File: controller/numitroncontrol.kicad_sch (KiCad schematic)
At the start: 10 parts, among them J0 Screw_Terminal_01x02, J1 Conn_01x06, J2 Conn_01x06, J3 RTC, J4 GPS, U1 LM317_TO-220

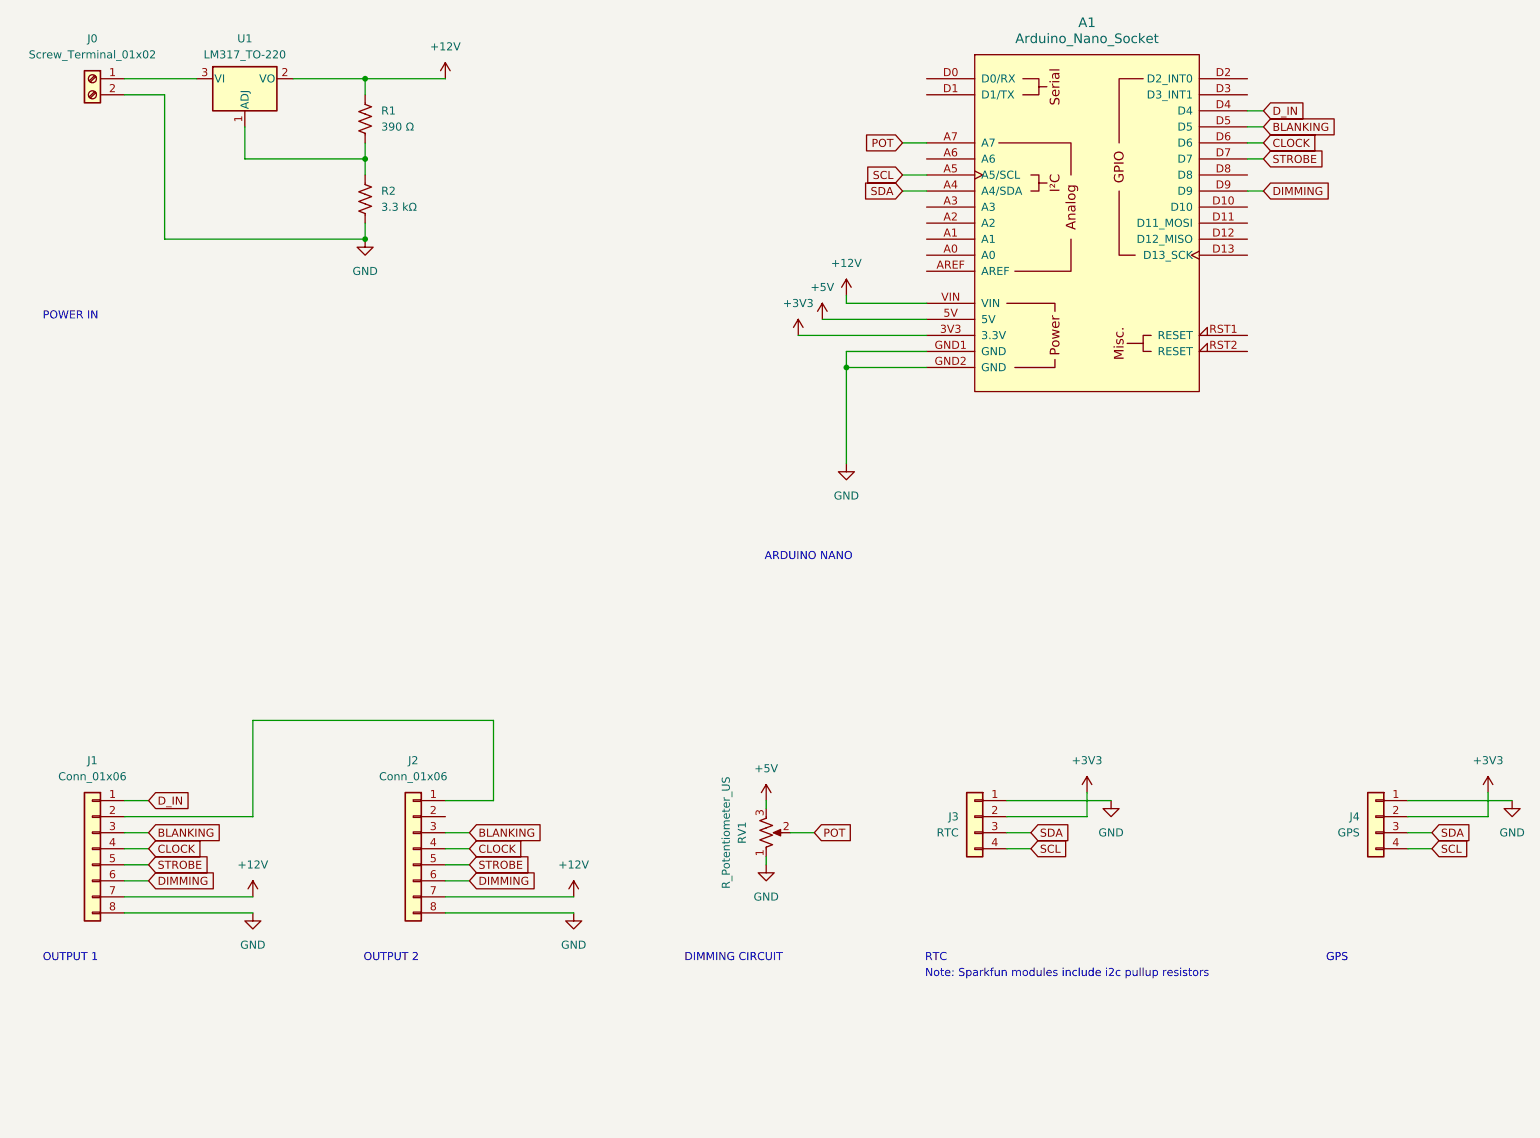
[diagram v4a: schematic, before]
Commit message: fixed serial communication pins
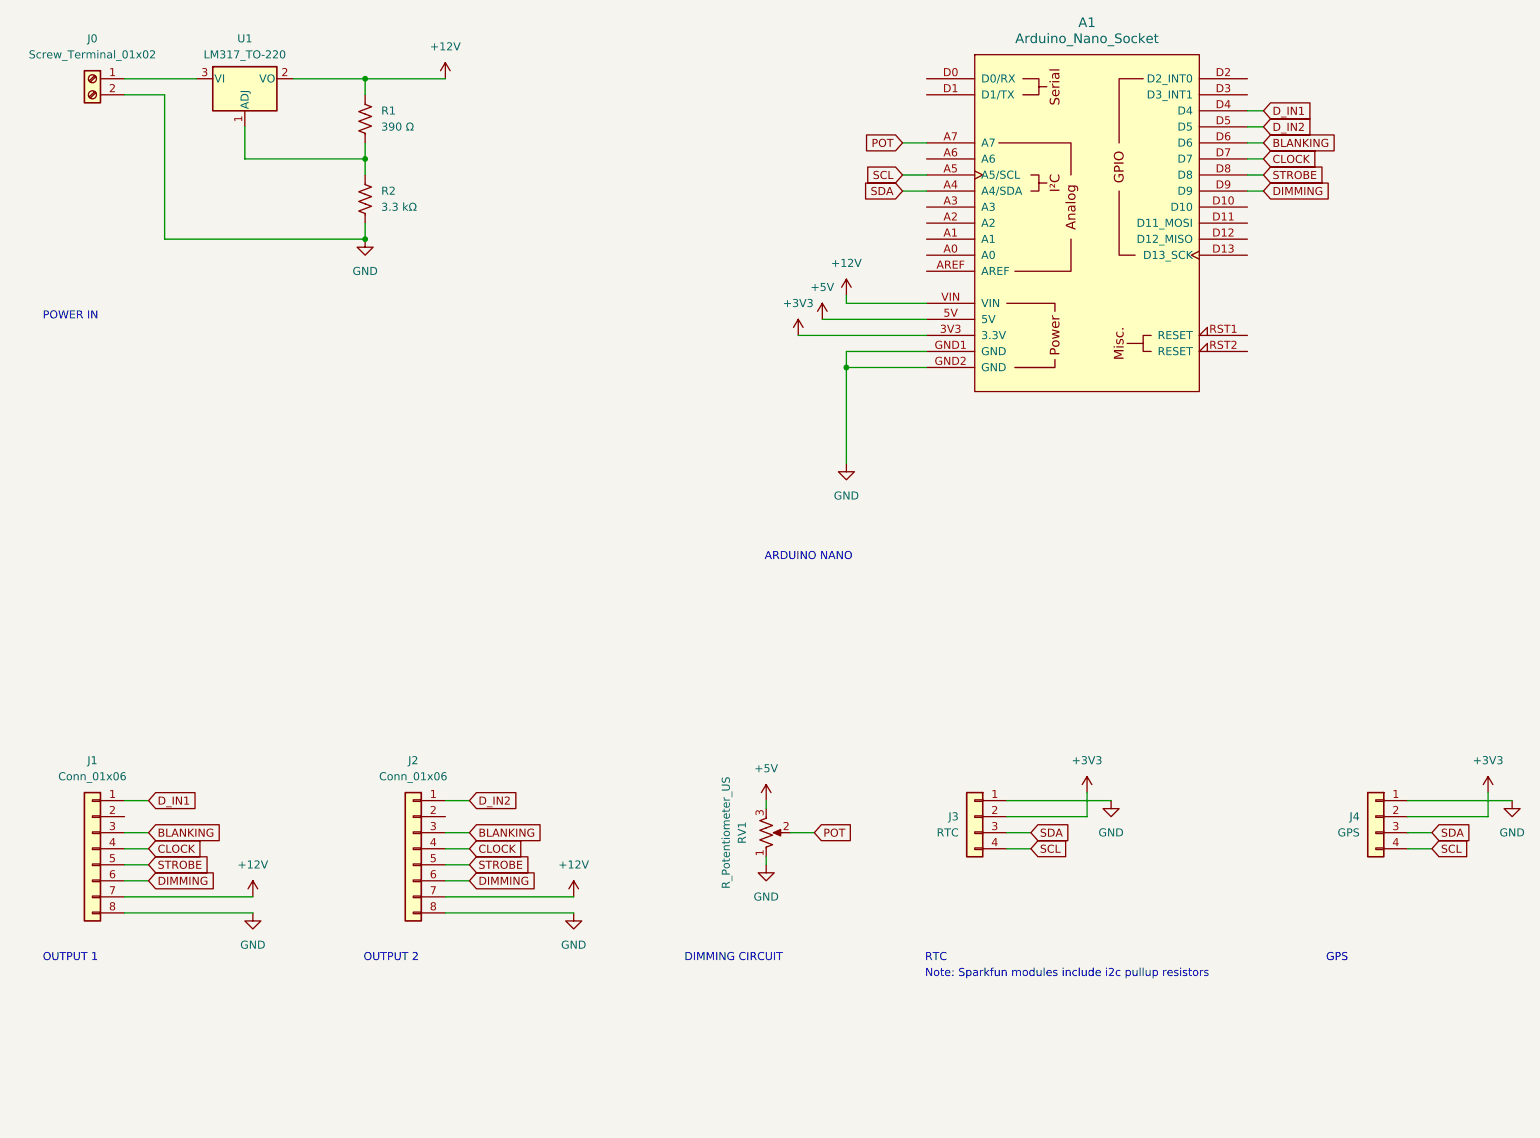
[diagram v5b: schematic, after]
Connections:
- net BLANKING: now also A1.D6; no longer A1.D5
- net CLOCK: now also A1.D7; no longer A1.D6
- net STROBE: now also A1.D8; no longer A1.D7
- net at J1.2 (Pin_2): no longer J2.1 (Pin_1)
- net D_IN renamed D_IN1
- new net D_IN2: A1.D5, J2.1 (Pin_1)

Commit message: updated control board
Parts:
- removed A1: Arduino_Nano_Socket, PCM_arduino-library:Arduino_Nano_Socket, symbol PCM_arduino-library:Arduino_Nano_Socket
- removed J4: GPS, Connector_PinHeader_2.54mm:PinHeader_1x04_P2.54mm_Vertical, symbol Connector_Generic:Conn_01x04
- added A1: Arduino_Nano_RP2040_Connect_Socket, PCM_arduino-library:Arduino_Nano_Every_Socket, symbol PCM_arduino-library:Arduino_Nano_RP2040_Connect_Socket
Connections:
- net +12V: now also A1.VIN
- net +3V3: now also A1.3V3 (3.3V)
- net +5V: now also A1.5V
- net BLANKING: now also A1.D6
- net CLOCK: now also A1.D7
- net DIMMING: now also A1.D9
- net D_IN1: now also A1.D4
- net D_IN2: now also A1.D5
- net GND: now also A1.GND1 (GND), A1.GND2 (GND)
- net POT: now also A1.A7
- net SCL: now also A1.A5 (A5/SCL)
- net SDA: now also A1.A4 (A4/SDA)
- net STROBE: now also A1.D8
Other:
- note added: "I2C"
- note removed: "GPS"
- note removed: "RTC"

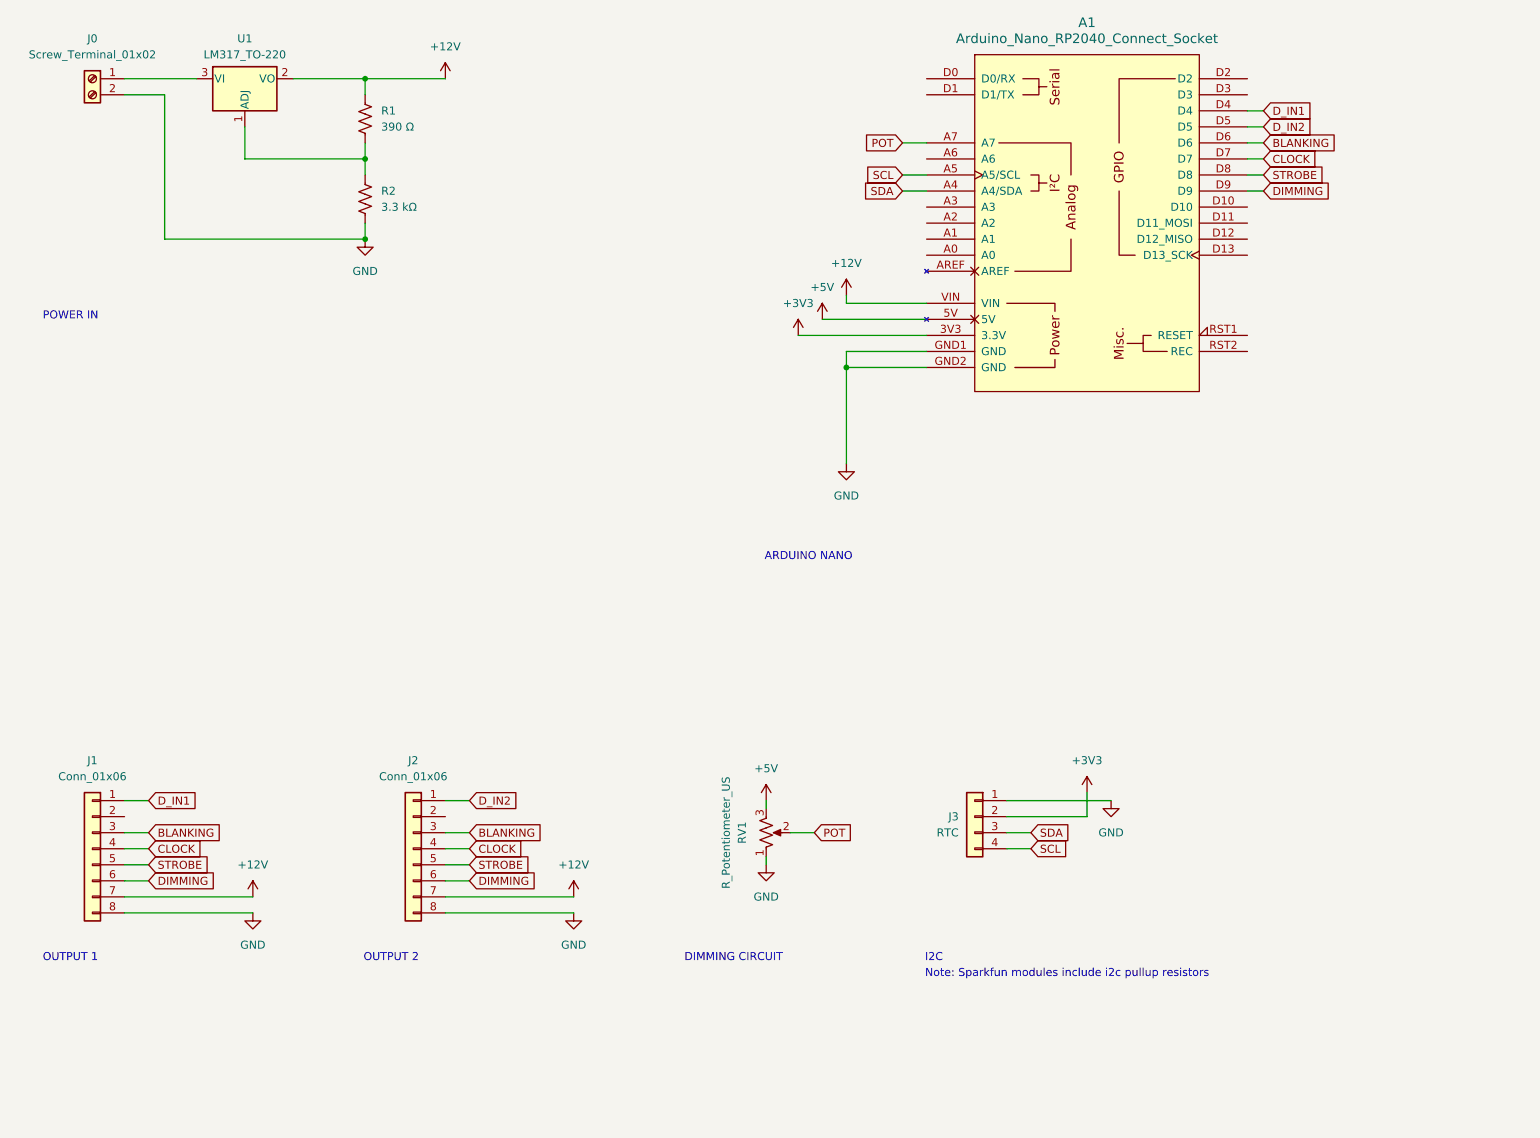
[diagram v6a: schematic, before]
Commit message: replaced pot with screw terminal for flexible mounting
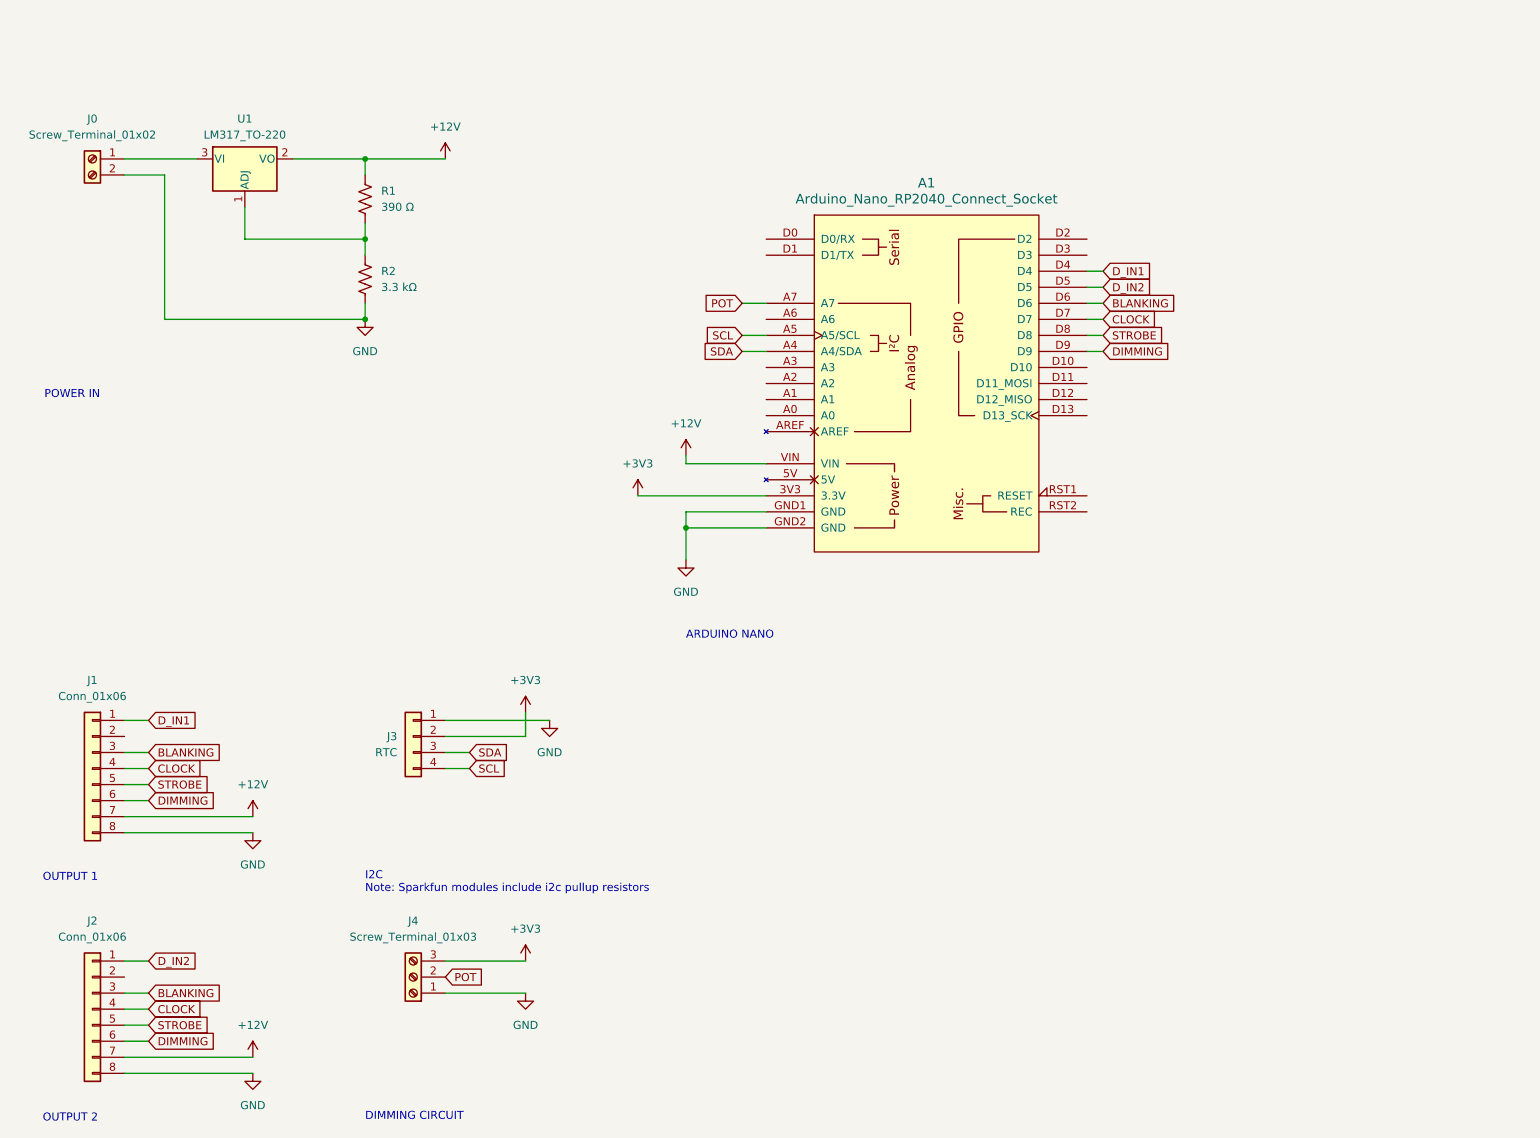
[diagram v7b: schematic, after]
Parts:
- removed RV1: R_Potentiometer_US, Connector_PinHeader_2.54mm:PinHeader_1x03_P2.54mm_Vertical, symbol Device:R_Potentiometer_US
- added J4: Screw_Terminal_01x03, TerminalBlock_4Ucon:TerminalBlock_4Ucon_1x03_P3.50mm_Horizontal, symbol Connector:Screw_Terminal_01x03
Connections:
- net +3V3: now also J4.3 (Pin_3)
- net GND: now also J4.1 (Pin_1)
- net POT: now also J4.2 (Pin_2)
- net +5V: no longer names the net of A1.5V
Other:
- moved on the sheet: A1, J0, J1, J2, J3, R1, R2, U1
